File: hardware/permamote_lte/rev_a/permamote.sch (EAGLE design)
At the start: 105 parts, among them IC1 NRF9160, J1 TC2030-JLINK-NL, J2 U.FL-R-SMT, J3 NANO_SIM, J4 U.FL-R-SMT, Q1 PMDXB950UPEL, Q10 PMDXB950UPEL, Q2 PMDXB950UPEL, Q3 PMDXB950UPEL, Q4 PMDXB950UPEL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

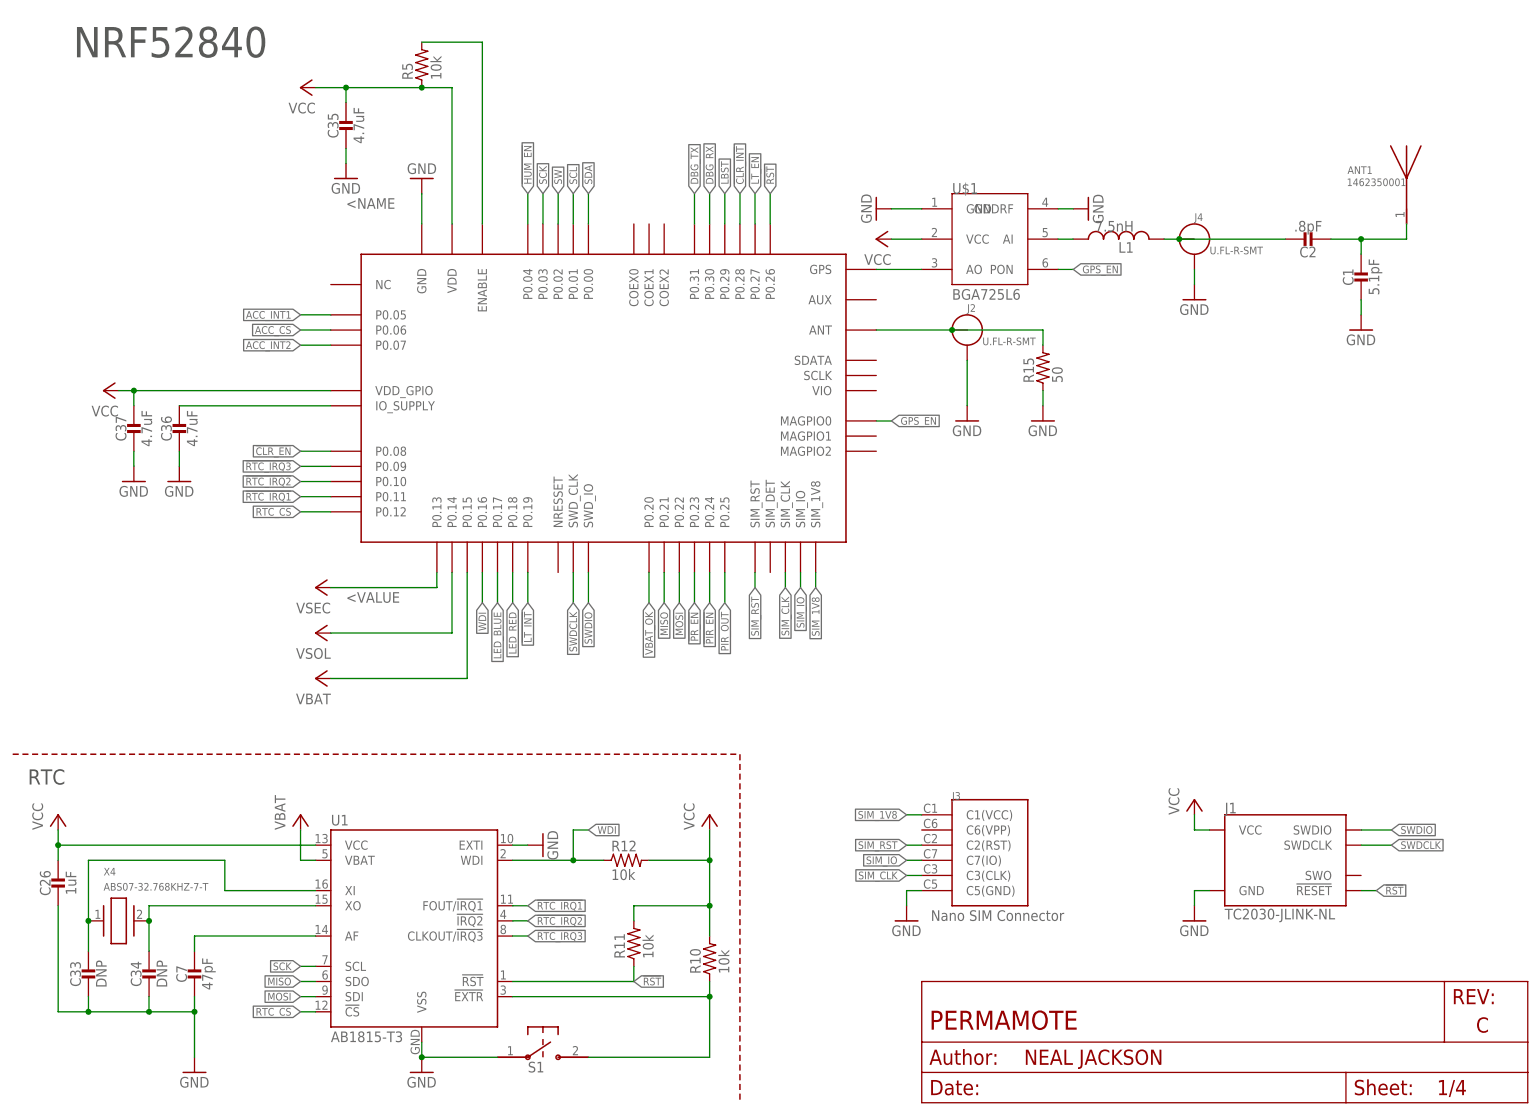
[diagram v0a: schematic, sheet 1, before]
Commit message: made revisions from schematic review
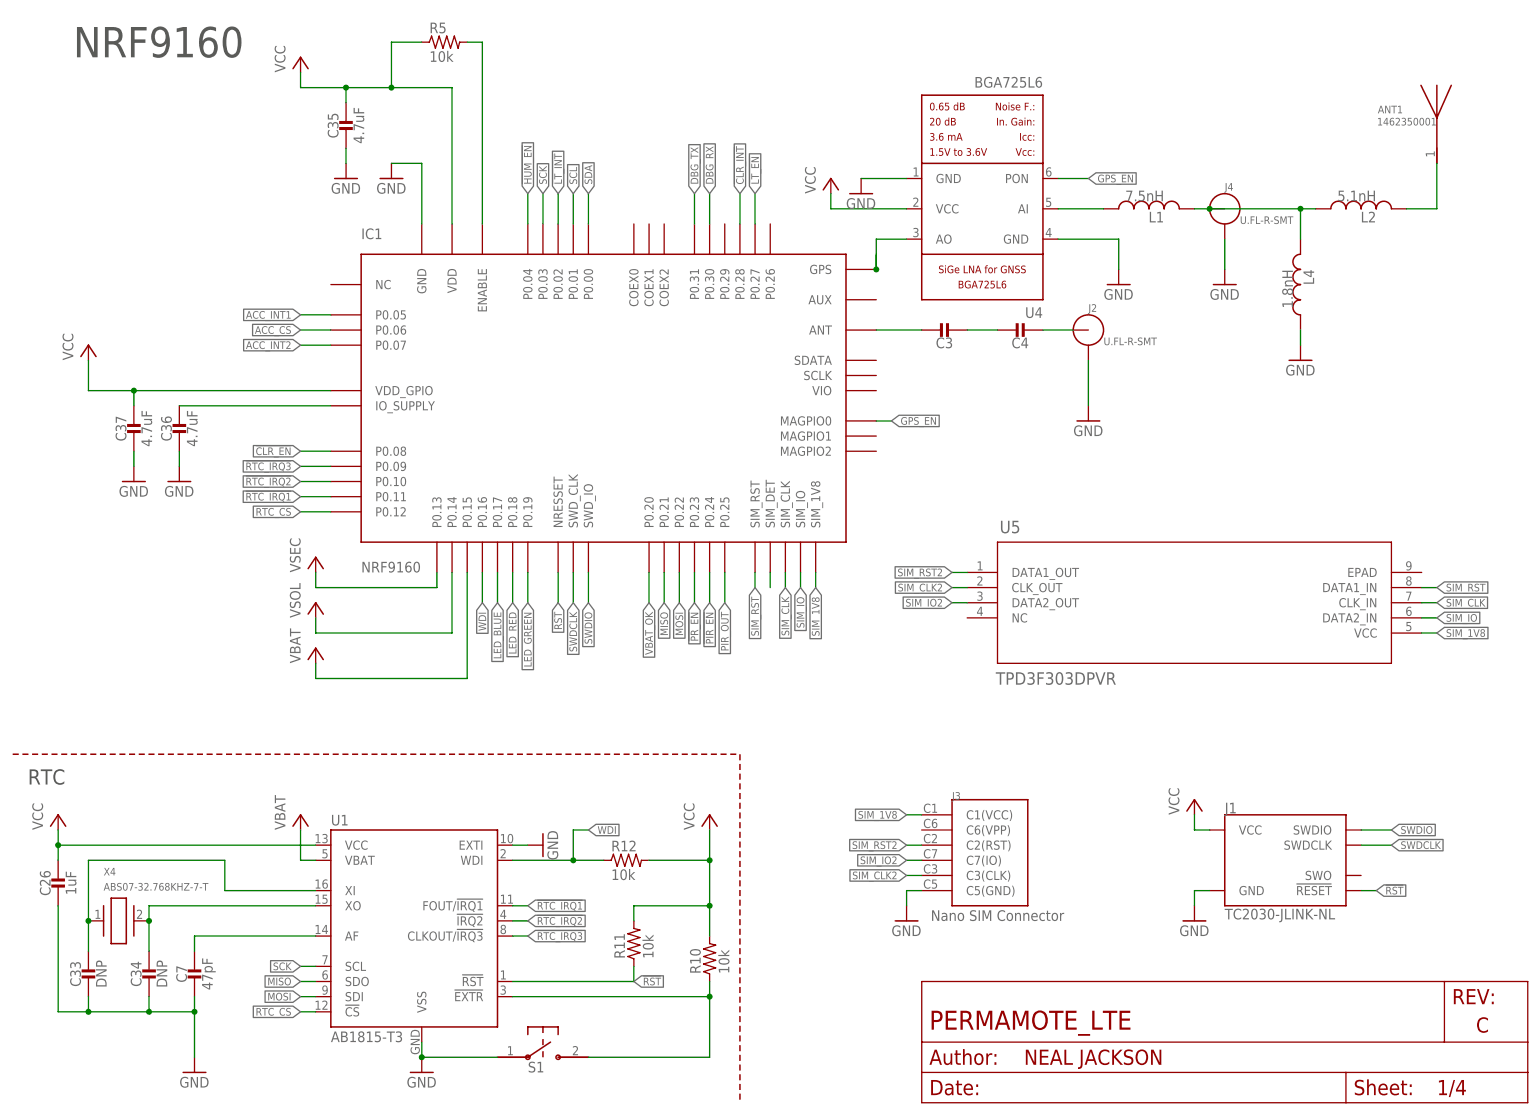
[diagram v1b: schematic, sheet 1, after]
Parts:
- removed C1: 5.1pF, passives:CAPACITOR0402_CAP
- removed C2: .8pF, passives:CAPACITOR0402_CAP
- removed R15: 50, passives:RESISTOR0402_RES
- removed U$1: BGA725L6, permamote:BGA725L6
- added C3, C4: (no value), passives:CAPACITOR0402_CAP
- added L2: 5.1nH, passives:INDUCTOR0402
- added L4: 1.8nH, passives:INDUCTOR0402
- added U4: BGA725L6, Particle:BGA725L6
- added U5: TPD3F303DPVR, TPD3F303:TPD3F303DPVR
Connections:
- removed net N$30: IC1.ANT, J2.ANT, R15.2
- removed net N$36: IC1.SIM_IO
- removed net N$37: IC1.SIM_CLK
- new net N$11: C4.2, J2.ANT
- new net N$40: J3.C2(RST)
- new net N$6: U4.PON
- new net N$7: C37.1, IC1.VDD_GPIO
- new net N$8: C3.2, C4.1
- new net N$9: C3.1, IC1.ANT
- new net SIM_CLK2: J3.C3(CLK), U5.CLK_OUT
- new net SIM_IO2: J3.C7(IO), U5.DATA2_OUT
- new net SIM_RST2: U5.DATA1_OUT
- net !LT_INT: now also IC1.P0.02; no longer IC1.P0.19
- net !RST: now also IC1.NRESSET; no longer IC1.P0.26
- net GND: now also L4.1, U4.GND@1, U4.GND@4; no longer C1.2, R15.1, U$1.GND, U$1.GNDRF
- net LBST: no longer IC1.P0.29
- net LED_GREEN: now also IC1.P0.19
- net N$1: now also U4.AO; no longer U$1.AO
- net N$2: now also U4.AI; no longer U$1.AI
- net N$3: now also IC1.SIM_DET; no longer U$1.PON
- net N$4: now also L2.1, L4.2; no longer C2.1
- net N$5: now also L2.2; no longer C1.1, C2.2
- net SIM_1V8: now also U5.VCC
- net SIM_CLK: now also IC1.SIM_CLK, U5.CLK_IN; no longer J3.C3(CLK)
- net SIM_IO: now also IC1.SIM_IO, U5.DATA2_IN; no longer J3.C7(IO)
- net SIM_RST: now also U5.DATA1_IN; no longer J3.C2(RST)
- net SW: no longer IC1.P0.02
- net VCC: now also U4.VCC; no longer C37.1, IC1.VDD_GPIO, U$1.VCC
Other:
- note added: "NRF9160"
- note removed: "NRF52840"
- note removed: "Only populate one MCU! Either populate the NRF52840 (Page 1) or NRF51822 (Page 2)"
- moved on the sheet: ANT1, J2, J4, L1, R5

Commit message: added sd card
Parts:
- added C1: 4.7uF, passives:CAPACITOR0402_CAP
- added J5: DM3AT-SF-PEJM5, connector:DM3AT-SF-PEJM5
- added R15, R6, R7: 10k, passives:RESISTOR0402_RES
- added R16, R19: 100k, passives:RESISTOR0402_RES
- added TP28, TP29, TP38: TEST_POINT_0.040IN, headers:TEST_POINT_0.040IN
- added U10: SIP32510, chips:SIP32510
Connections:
- new net !SD_CS: IC1.P0.26, J5.DATA3-CD/CS_N, R6.1
- new net !SD_DETECT: IC1.P0.27, J5.A, R16.1, TP38.TESTPOINT
- new net +3V3: R19.2, U10.VSUPP
- new net N$13: C1.1, J5.VCC, R15.2, R16.2, R6.2, R7.2, U10.VLOAD
- new net SD_ENABLE: IC1.P0.28, R19.1, U10.EN
- net !CLR_INT: now also IC1.P0.29; no longer IC1.P0.28
- net !LT_EN: now also IC1.P0.09; no longer IC1.P0.27
- net !RTC_IRQ3: no longer IC1.P0.09
- net GND: now also C1.2, J5.B, J5.GND, U10.GND
- net MISO: now also J5.DATA0/MISO, R15.1
- net MOSI: now also J5.CMD/MOSI, R7.1
- net SCK: now also J5.CLK
- net SIM_IO2: now also TP28.TESTPOINT
- net SIM_RST2: now also TP29.TESTPOINT
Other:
- note added: "SD Card Adapter"

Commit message: sch tweaks
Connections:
- removed net DBG_RX: IC1.P0.30
- removed net DBG_TX: IC1.P0.31
- net !CLR_EN: now also IC1.P0.30; no longer IC1.P0.08
- net !CLR_INT: now also IC1.P0.20; no longer IC1.P0.29
- net !HUM_EN: now also IC1.P0.17; no longer IC1.P0.04
- net !LT_EN: now also IC1.P0.18; no longer IC1.P0.09
- net !LT_INT: now also IC1.P0.04; no longer IC1.P0.02
- net !RTC_IRQ1: now also IC1.P0.09; no longer IC1.P0.11
- net !RTC_IRQ2: now also IC1.P0.11; no longer IC1.P0.10
- net !RTC_IRQ3: now also IC1.P0.10
- net LED_BLUE: now also IC1.P0.01; no longer IC1.P0.17
- net LED_GREEN: now also IC1.P0.02; no longer IC1.P0.19
- net LED_RED: now also IC1.P0.00; no longer IC1.P0.18
- net SCL: now also IC1.P0.19; no longer IC1.P0.01
- net SDA: now also IC1.P0.08; no longer IC1.P0.00
- net VBAT_OK: now also IC1.P0.29; no longer IC1.P0.20

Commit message: layout
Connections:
- net !CLR_EN: now also IC1.P0.08; no longer IC1.P0.30
- net !CLR_INT: now also IC1.P0.29; no longer IC1.P0.20
- net !HUM_EN: now also IC1.P0.04; no longer IC1.P0.17
- net !LT_EN: now also IC1.P0.30; no longer IC1.P0.18
- net !LT_INT: now also IC1.P0.02; no longer IC1.P0.04
- net !RTC_IRQ1: now also IC1.P0.11; no longer IC1.P0.09
- net !RTC_IRQ2: now also IC1.P0.10; no longer IC1.P0.11
- net !RTC_IRQ3: now also IC1.P0.09; no longer IC1.P0.10
- net LED_BLUE: now also IC1.P0.17; no longer IC1.P0.01
- net LED_GREEN: now also IC1.P0.19; no longer IC1.P0.02
- net LED_RED: now also IC1.P0.18; no longer IC1.P0.00
- net SCL: now also IC1.P0.01; no longer IC1.P0.19
- net SDA: now also IC1.P0.00; no longer IC1.P0.08
- net VBAT_OK: now also IC1.P0.20; no longer IC1.P0.29
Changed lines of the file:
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@@
 <part name="J4" library="connector" deviceset="U.FL-R-SMT" device=""/>
 <part name="GND28" library="supply1" library_urn="urn:adsk.eagle:library:371" deviceset="GND" device=""/>
+<part name="ANT1" library="1462350001" deviceset="1462350001" device=""/>
 <part name="BAT1" library="batteries" deviceset="2477THMCOINCELLCLIP" device=""/>
 <part name="GND32" library="supply1" library_urn="urn:adsk.eagle:library:371" deviceset="GND" device=""/>
@@
 <part name="TP28" library="headers" deviceset="TEST_POINT_0.040IN" device=""/>
 <part name="TP29" library="headers" deviceset="TEST_POINT_0.040IN" device=""/>
-<part name="ANT1" library="1462350001" deviceset="1462350001" device=""/>
 </parts>
 <sheets>
@@
 <attribute name="VALUE" x="200.66" y="134.62" size="1.778" layer="96"/>
 </instance>
+<instance part="ANT1" gate="G$1" x="238.76" y="162.56" smashed="yes">
+<attribute name="NAME" x="228.86041875" y="165.869590625" size="1.27291875" layer="95"/>
+<attribute name="VALUE" x="228.7332" y="163.83295" size="1.27295" layer="96"/>
+</instance>
 <instance part="GND32" gate="1" x="88.9" y="43.18" smashed="yes" rot="R90">
 <attribute name="VALUE" x="91.44" y="40.64" size="1.778" layer="96" rot="R90"/>
@@
 <attribute name="NAME" x="216.408" y="139.7" size="1.778" layer="95" ratio="12" rot="R270"/>
 <attribute name="VALUE" x="212.852" y="139.7" size="1.778" layer="96" ratio="12" rot="R270"/>
-</instance>
-<instance part="ANT1" gate="G$1" x="238.76" y="162.56" smashed="yes">
-<attribute name="NAME" x="228.86041875" y="165.869590625" size="1.27291875" layer="95"/>
-<attribute name="VALUE" x="228.7332" y="163.83295" size="1.27295" layer="96"/>
 </instance>
 </instances>
@@
 </segment>
 </net>
+<net name="SCL" class="0">
+<segment>
+<label x="93.98" y="152.4" size="1.27" layer="95" rot="R90" xref="yes"/>
+<wire x1="93.98" y1="147.32" x2="93.98" y2="152.4" width="0.1524" layer="91"/>
+<pinref part="IC1" gate="G$1" pin="P0.01"/>
+</segment>
+</net>
+<net name="SDA" class="0">
+<segment>
+<label x="96.52" y="152.4" size="1.27" layer="95" rot="R90" xref="yes"/>
+<wire x1="96.52" y1="147.32" x2="96.52" y2="152.4" width="0.1524" layer="91"/>
+<pinref part="IC1" gate="G$1" pin="P0.00"/>
+</segment>
+</net>
 <net name="N$25" class="0">
 <segment>
@@
 </segment>
 <segment>
-<pinref part="IC1" gate="G$1" pin="P0.09"/>
-<wire x1="53.34" y1="106.68" x2="48.26" y2="106.68" width="0.1524" layer="91"/>
-<label x="48.26" y="106.68" size="1.27" layer="95" rot="R180" xref="yes"/>
+<label x="48.26" y="101.6" size="1.27" layer="95" rot="R180" xref="yes"/>
+<wire x1="48.26" y1="101.6" x2="53.34" y2="101.6" width="0.1524" layer="91"/>
+<pinref part="IC1" gate="G$1" pin="P0.11"/>
 </segment>
 </net>
@@
 </segment>
 <segment>
-<label x="48.26" y="101.6" size="1.27" layer="95" rot="R180" xref="yes"/>
-<wire x1="48.26" y1="101.6" x2="53.34" y2="101.6" width="0.1524" layer="91"/>
-<pinref part="IC1" gate="G$1" pin="P0.11"/>
+<label x="48.26" y="104.14" size="1.27" layer="95" rot="R180" xref="yes"/>
+<wire x1="48.26" y1="104.14" x2="53.34" y2="104.14" width="0.1524" layer="91"/>
+<pinref part="IC1" gate="G$1" pin="P0.10"/>
 </segment>
 </net>
@@
 </segment>
 </net>
+<net name="!CLR_INT" class="0">
+<segment>
+<label x="119.38" y="152.4" size="1.27" layer="95" rot="R90" xref="yes"/>
+<pinref part="IC1" gate="G$1" pin="P0.29"/>
+<wire x1="119.38" y1="152.4" x2="119.38" y2="147.32" width="0.1524" layer="91"/>
+</segment>
+</net>
 <net name="!LT_INT" class="0">
 <segment>
-<label x="86.36" y="152.4" size="1.27" layer="95" rot="R90" xref="yes"/>
-<pinref part="IC1" gate="G$1" pin="P0.04"/>
-<wire x1="86.36" y1="152.4" x2="86.36" y2="147.32" width="0.1524" layer="91"/>
+<label x="91.44" y="152.4" size="1.27" layer="95" rot="R90" xref="yes"/>
+<wire x1="91.44" y1="147.32" x2="91.44" y2="152.4" width="0.1524" layer="91"/>
+<pinref part="IC1" gate="G$1" pin="P0.02"/>
 </segment>
 </net>
@@
 <net name="!CLR_EN" class="0">
 <segment>
-<pinref part="IC1" gate="G$1" pin="P0.30"/>
-<wire x1="116.84" y1="147.32" x2="116.84" y2="152.4" width="0.1524" layer="91"/>
-<label x="116.84" y="152.4" size="1.27" layer="95" rot="R90" xref="yes"/>
+<label x="48.26" y="109.22" size="1.27" layer="95" rot="R180" xref="yes"/>
+<wire x1="48.26" y1="109.22" x2="53.34" y2="109.22" width="0.1524" layer="91"/>
+<pinref part="IC1" gate="G$1" pin="P0.08"/>
 </segment>
 </net>
@@
 </segment>
 <segment>
-<label x="48.26" y="104.14" size="1.27" layer="95" rot="R180" xref="yes"/>
-<wire x1="48.26" y1="104.14" x2="53.34" y2="104.14" width="0.1524" layer="91"/>
-<pinref part="IC1" gate="G$1" pin="P0.10"/>
+<pinref part="IC1" gate="G$1" pin="P0.09"/>
+<wire x1="53.34" y1="106.68" x2="48.26" y2="106.68" width="0.1524" layer="91"/>
+<label x="48.26" y="106.68" size="1.27" layer="95" rot="R180" xref="yes"/>
 </segment>
 </net>
@@
 </segment>
 </net>
+<net name="!HUM_EN" class="0">
+<segment>
+<label x="86.36" y="152.4" size="1.27" layer="95" rot="R90" xref="yes"/>
+<wire x1="86.36" y1="152.4" x2="86.36" y2="147.32" width="0.1524" layer="91"/>
+<pinref part="IC1" gate="G$1" pin="P0.04"/>
+</segment>
+</net>
 <net name="!PR_EN" class="0">
 <segment>
@@
 <net name="!LT_EN" class="0">
 <segment>
+<label x="116.84" y="152.4" size="1.27" layer="95" rot="R90" xref="yes"/>
+<pinref part="IC1" gate="G$1" pin="P0.30"/>
+<wire x1="116.84" y1="152.4" x2="116.84" y2="147.32" width="0.1524" layer="91"/>
+</segment>
+</net>
+<net name="LED_RED" class="0">
+<segment>
+<label x="83.82" y="83.82" size="1.27" layer="95" rot="R270" xref="yes"/>
+<wire x1="83.82" y1="83.82" x2="83.82" y2="88.9" width="0.1524" layer="91"/>
 <pinref part="IC1" gate="G$1" pin="P0.18"/>
-<wire x1="83.82" y1="88.9" x2="83.82" y2="83.82" width="0.1524" layer="91"/>
-<label x="83.82" y="83.82" size="1.27" layer="95" rot="R270" xref="yes"/>
+</segment>
+</net>
+<net name="LED_BLUE" class="0">
+<segment>
+<label x="81.28" y="83.82" size="1.27" layer="95" rot="R270" xref="yes"/>
+<wire x1="81.28" y1="83.82" x2="81.28" y2="88.9" width="0.1524" layer="91"/>
+<pinref part="IC1" gate="G$1" pin="P0.17"/>
+</segment>
+</net>
+<net name="VBAT_OK" class="0">
+<segment>
+<label x="106.68" y="83.82" size="1.27" layer="95" rot="R270" xref="yes"/>
+<wire x1="106.68" y1="83.82" x2="106.68" y2="88.9" width="0.1524" layer="91"/>
+<pinref part="IC1" gate="G$1" pin="P0.20"/>
 </segment>
 </net>
@@
 <net name="N$5" class="0">
 <segment>
+<pinref part="ANT1" gate="G$1" pin="1"/>
 <wire x1="238.76" y1="149.86" x2="238.76" y2="157.48" width="0.1524" layer="91"/>
 <pinref part="L2" gate="G$1" pin="2"/>
 <wire x1="233.68" y1="149.86" x2="238.76" y2="149.86" width="0.1524" layer="91"/>
-<pinref part="ANT1" gate="G$1" pin="1"/>
+</segment>
+</net>
+<net name="LED_GREEN" class="0">
+<segment>
+<wire x1="86.36" y1="88.9" x2="86.36" y2="83.82" width="0.1524" layer="91"/>
+<label x="86.36" y="83.82" size="1.27" layer="95" rot="R270" xref="yes"/>
+<pinref part="IC1" gate="G$1" pin="P0.19"/>
 </segment>
 </net>
@@
 </segment>
 </net>
-<net name="!HUM_EN" class="0">
-<segment>
-<pinref part="IC1" gate="G$1" pin="P0.17"/>
-<wire x1="81.28" y1="88.9" x2="81.28" y2="83.82" width="0.1524" layer="91"/>
-<label x="81.28" y="83.82" size="1.27" layer="95" rot="R270" xref="yes"/>
-</segment>
-</net>
-<net name="LED_GREEN" class="0">
-<segment>
-<pinref part="IC1" gate="G$1" pin="P0.02"/>
-<wire x1="91.44" y1="147.32" x2="91.44" y2="152.4" width="0.1524" layer="91"/>
-<label x="91.44" y="152.4" size="1.27" layer="95" rot="R90" xref="yes"/>
-</segment>
-</net>
-<net name="LED_BLUE" class="0">
-<segment>
-<pinref part="IC1" gate="G$1" pin="P0.01"/>
-<wire x1="93.98" y1="147.32" x2="93.98" y2="152.4" width="0.1524" layer="91"/>
-<label x="93.98" y="152.4" size="1.27" layer="95" rot="R90" xref="yes"/>
-</segment>
-</net>
-<net name="!CLR_INT" class="0">
-<segment>
-<pinref part="IC1" gate="G$1" pin="P0.20"/>
-<wire x1="106.68" y1="88.9" x2="106.68" y2="83.82" width="0.1524" layer="91"/>
-<label x="106.68" y="83.82" size="1.27" layer="95" rot="R270" xref="yes"/>
-</segment>
-</net>
-<net name="VBAT_OK" class="0">
-<segment>
-<pinref part="IC1" gate="G$1" pin="P0.29"/>
-<wire x1="119.38" y1="147.32" x2="119.38" y2="152.4" width="0.1524" layer="91"/>
-<label x="119.38" y="152.4" size="1.27" layer="95" rot="R90" xref="yes"/>
-</segment>
-</net>
-<net name="LED_RED" class="0">
-<segment>
-<pinref part="IC1" gate="G$1" pin="P0.00"/>
-<wire x1="96.52" y1="147.32" x2="96.52" y2="152.4" width="0.1524" layer="91"/>
-<label x="96.52" y="152.4" size="1.27" layer="95" rot="R90" xref="yes"/>
-</segment>
-</net>
-<net name="SDA" class="0">
-<segment>
-<label x="48.26" y="109.22" size="1.27" layer="95" rot="R180" xref="yes"/>
-<pinref part="IC1" gate="G$1" pin="P0.08"/>
-<wire x1="48.26" y1="109.22" x2="53.34" y2="109.22" width="0.1524" layer="91"/>
-</segment>
-</net>
-<net name="SCL" class="0">
-<segment>
-<pinref part="IC1" gate="G$1" pin="P0.19"/>
-<wire x1="86.36" y1="88.9" x2="86.36" y2="83.82" width="0.1524" layer="91"/>
-<label x="86.36" y="83.82" size="1.27" layer="95" rot="R270" xref="yes"/>
-</segment>
-</net>
